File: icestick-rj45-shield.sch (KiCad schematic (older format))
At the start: 0 parts

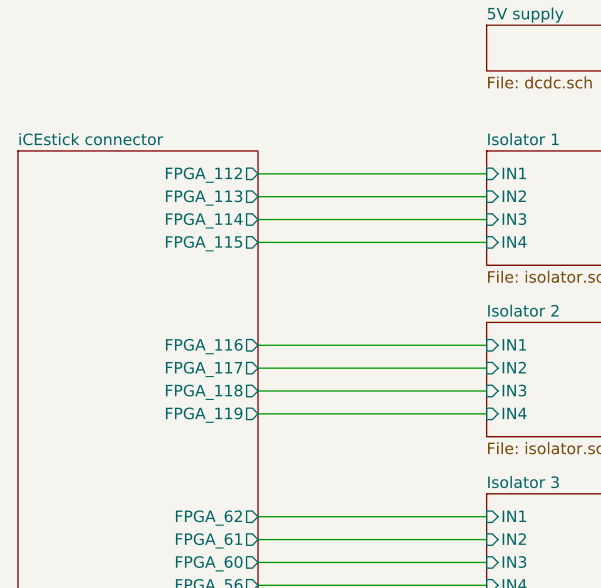
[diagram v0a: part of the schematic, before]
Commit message: Continued layouting
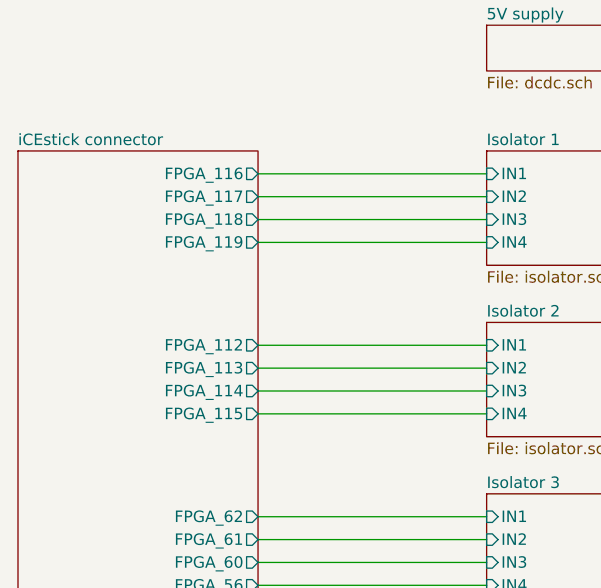
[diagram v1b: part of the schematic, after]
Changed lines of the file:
@@
 F0 "iCEstick connector" 50
 F1 "icestick.sch" 50
-F2 "FPGA_112" O R 4800 2500 50
-F3 "FPGA_113" O R 4800 2600 50
-F4 "FPGA_114" O R 4800 2700 50
-F5 "FPGA_115" O R 4800 2800 50
-F6 "FPGA_116" O R 4800 3250 50
-F7 "FPGA_117" O R 4800 3350 50
-F8 "FPGA_118" O R 4800 3450 50
-F9 "FPGA_119" O R 4800 3550 50
+F2 "FPGA_112" O R 4800 3250 50
+F3 "FPGA_113" O R 4800 3350 50
+F4 "FPGA_114" O R 4800 3450 50
+F5 "FPGA_115" O R 4800 3550 50
+F6 "FPGA_116" O R 4800 2500 50
+F7 "FPGA_117" O R 4800 2600 50
+F8 "FPGA_118" O R 4800 2700 50
+F9 "FPGA_119" O R 4800 2800 50
 F10 "FPGA_62" O R 4800 4000 50
 F11 "FPGA_61" O R 4800 4100 50

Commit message: Routed all the signals
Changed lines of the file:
@@
 F4 "FPGA_114" O R 4800 3450 50
 F5 "FPGA_115" O R 4800 3550 50
-F6 "FPGA_116" O R 4800 2500 50
-F7 "FPGA_117" O R 4800 2600 50
-F8 "FPGA_118" O R 4800 2700 50
-F9 "FPGA_119" O R 4800 2800 50
-F10 "FPGA_62" O R 4800 4000 50
-F11 "FPGA_61" O R 4800 4100 50
-F12 "FPGA_60" O R 4800 4200 50
-F13 "FPGA_56" O R 4800 4300 50
+F6 "FPGA_116" O R 4800 2800 50
+F7 "FPGA_117" O R 4800 2700 50
+F8 "FPGA_118" O R 4800 2600 50
+F9 "FPGA_119" O R 4800 2500 50
+F10 "FPGA_62" O R 4800 4300 50
+F11 "FPGA_61" O R 4800 4200 50
+F12 "FPGA_60" O R 4800 4100 50
+F13 "FPGA_56" O R 4800 4000 50
 F14 "FPGA_48" O R 4800 4750 50
 F15 "FPGA_47" O R 4800 4850 50

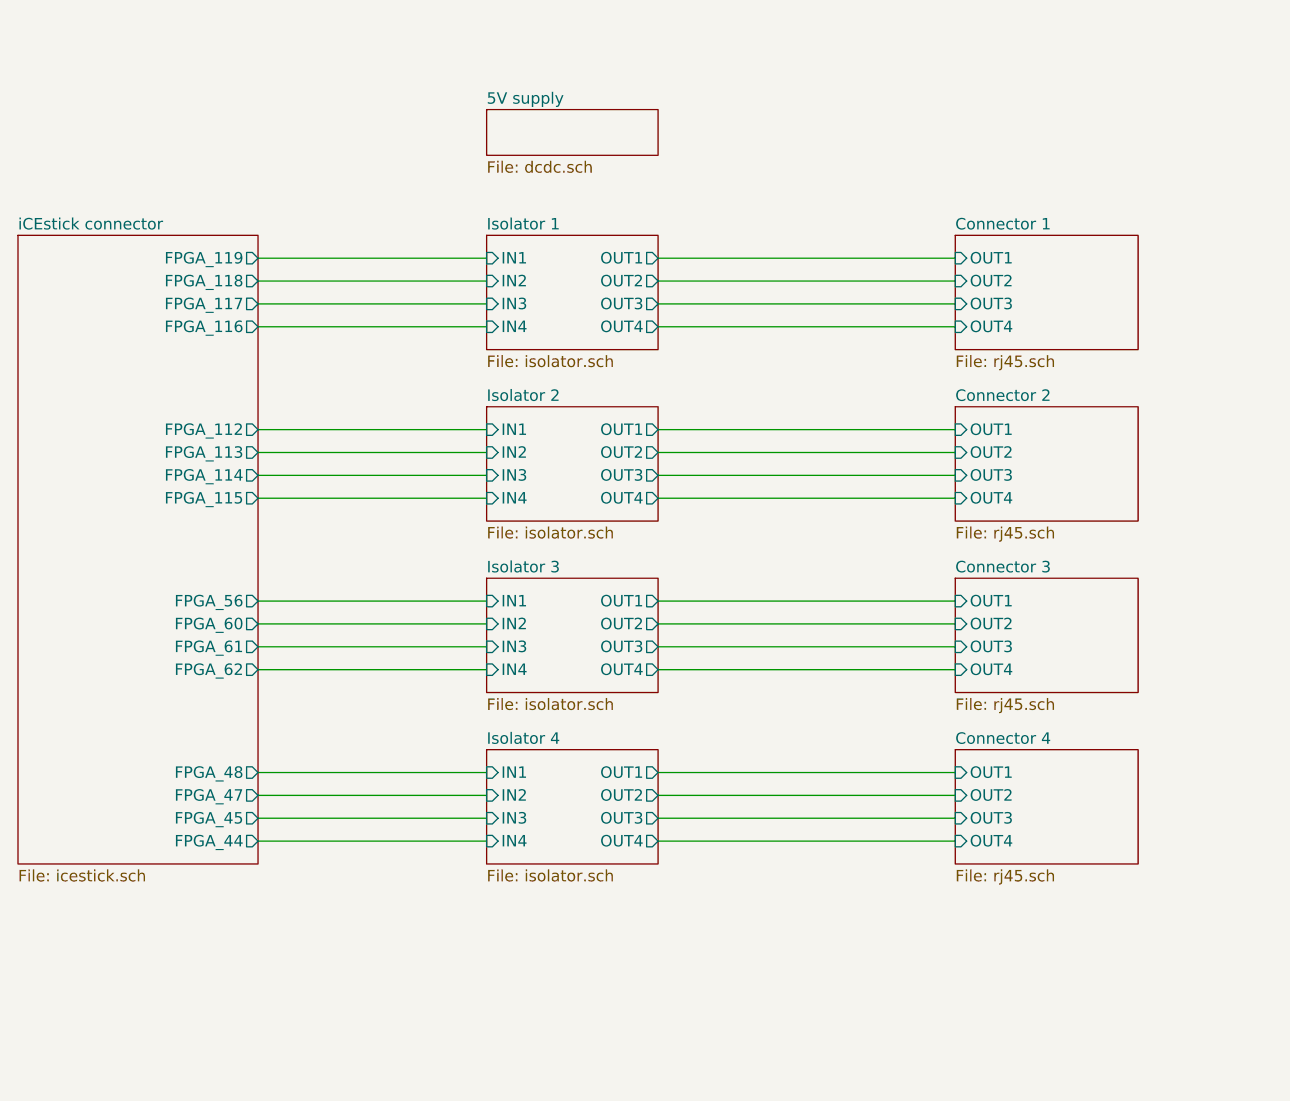
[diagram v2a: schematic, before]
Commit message: Updated RJ45 symbol and corresponding signal names
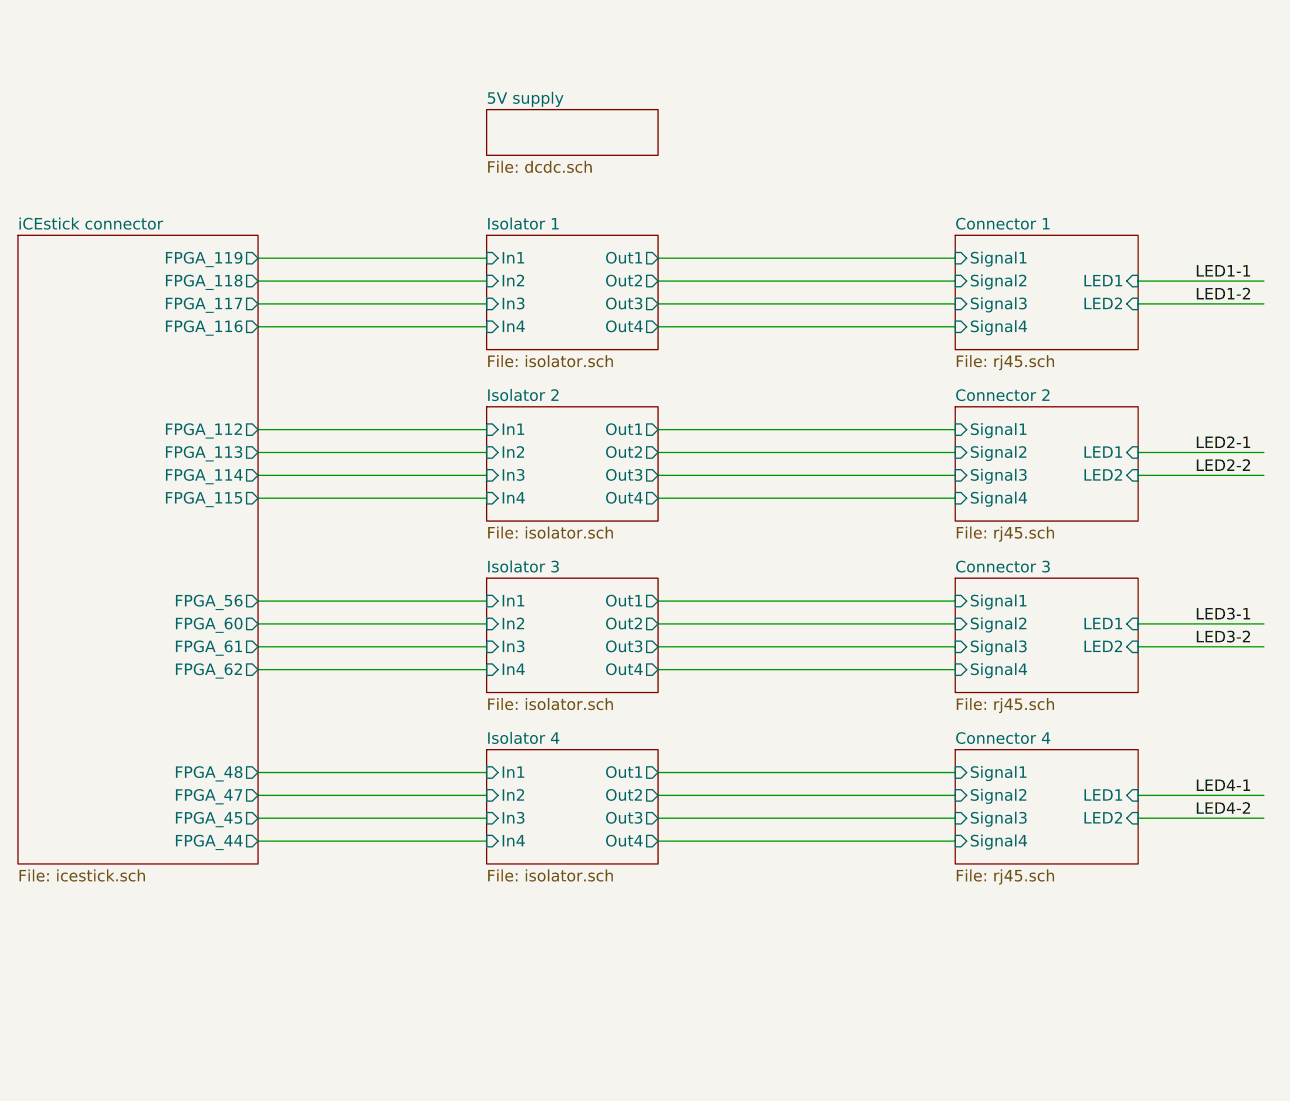
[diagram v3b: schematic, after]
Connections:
- net labels added: LED1-1, LED1-2, LED2-1, LED2-2, LED3-1, LED3-2, LED4-1, LED4-2
- wire segments 32 -> 40
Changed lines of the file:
@@
 F0 "Isolator 1" 50
 F1 "isolator.sch" 50
-F2 "IN1" I L 5800 2500 50
-F3 "IN2" I L 5800 2600 50
-F4 "OUT1" O R 6550 2500 50
-F5 "OUT2" O R 6550 2600 50
-F6 "OUT3" O R 6550 2700 50
-F7 "OUT4" O R 6550 2800 50
-F8 "IN3" I L 5800 2700 50
-F9 "IN4" I L 5800 2800 50
+F2 "In1" I L 5800 2500 50
+F3 "In2" I L 5800 2600 50
+F4 "Out1" O R 6550 2500 50
+F5 "Out2" O R 6550 2600 50
+F6 "Out3" O R 6550 2700 50
+F7 "Out4" O R 6550 2800 50
+F8 "In3" I L 5800 2700 50
+F9 "In4" I L 5800 2800 50
 $EndSheet
 $Sheet
@@
 F0 "Isolator 3" 50
 F1 "isolator.sch" 50
-F2 "IN1" I L 5800 4000 50
-F3 "IN2" I L 5800 4100 50
-F4 "OUT1" O R 6550 4000 50
-F5 "OUT2" O R 6550 4100 50
-F6 "OUT3" O R 6550 4200 50
-F7 "OUT4" O R 6550 4300 50
-F8 "IN3" I L 5800 4200 50
-F9 "IN4" I L 5800 4300 50
+F2 "In1" I L 5800 4000 50
+F3 "In2" I L 5800 4100 50
+F4 "Out1" O R 6550 4000 50
+F5 "Out2" O R 6550 4100 50
+F6 "Out3" O R 6550 4200 50
+F7 "Out4" O R 6550 4300 50
+F8 "In3" I L 5800 4200 50
+F9 "In4" I L 5800 4300 50
 $EndSheet
 $Sheet
@@
 F0 "Isolator 2" 50
 F1 "isolator.sch" 50
-F2 "IN1" I L 5800 3250 50
-F3 "IN2" I L 5800 3350 50
-F4 "OUT1" O R 6550 3250 50
-F5 "OUT2" O R 6550 3350 50
-F6 "OUT3" O R 6550 3450 50
-F7 "OUT4" O R 6550 3550 50
-F8 "IN3" I L 5800 3450 50
-F9 "IN4" I L 5800 3550 50
+F2 "In1" I L 5800 3250 50
+F3 "In2" I L 5800 3350 50
+F4 "Out1" O R 6550 3250 50
+F5 "Out2" O R 6550 3350 50
+F6 "Out3" O R 6550 3450 50
+F7 "Out4" O R 6550 3550 50
+F8 "In3" I L 5800 3450 50
+F9 "In4" I L 5800 3550 50
 $EndSheet
 $Sheet
@@
 F0 "Isolator 4" 50
 F1 "isolator.sch" 50
-F2 "IN1" I L 5800 4750 50
-F3 "IN2" I L 5800 4850 50
-F4 "OUT1" O R 6550 4750 50
-F5 "OUT2" O R 6550 4850 50
-F6 "OUT3" O R 6550 4950 50
-F7 "OUT4" O R 6550 5050 50
-F8 "IN3" I L 5800 4950 50
-F9 "IN4" I L 5800 5050 50
+F2 "In1" I L 5800 4750 50
+F3 "In2" I L 5800 4850 50
+F4 "Out1" O R 6550 4750 50
+F5 "Out2" O R 6550 4850 50
+F6 "Out3" O R 6550 4950 50
+F7 "Out4" O R 6550 5050 50
+F8 "In3" I L 5800 4950 50
+F9 "In4" I L 5800 5050 50
 $EndSheet
 Wire Wire Line
@@
 F0 "Connector 1" 50
 F1 "rj45.sch" 50
-F2 "OUT1" I L 7850 2500 50
-F3 "OUT2" I L 7850 2600 50
-F4 "OUT3" I L 7850 2700 50
-F5 "OUT4" I L 7850 2800 50
+F2 "Signal1" I L 7850 2500 50
+F3 "Signal2" I L 7850 2600 50
+F4 "Signal3" I L 7850 2700 50
+F5 "Signal4" I L 7850 2800 50
+F6 "LED1" I R 8650 2600 50
+F7 "LED2" I R 8650 2700 50
 $EndSheet
 Wire Wire Line
@@
 F0 "Connector 2" 50
 F1 "rj45.sch" 50
-F2 "OUT1" I L 7850 3250 50
-F3 "OUT2" I L 7850 3350 50
-F4 "OUT3" I L 7850 3450 50
-F5 "OUT4" I L 7850 3550 50
+F2 "Signal1" I L 7850 3250 50
+F3 "Signal2" I L 7850 3350 50
+F4 "Signal3" I L 7850 3450 50
+F5 "Signal4" I L 7850 3550 50
+F6 "LED1" I R 8650 3350 50
+F7 "LED2" I R 8650 3450 50
 $EndSheet
 Wire Wire Line
@@
 F0 "Connector 3" 50
 F1 "rj45.sch" 50
-F2 "OUT1" I L 7850 4000 50
-F3 "OUT2" I L 7850 4100 50
-F4 "OUT3" I L 7850 4200 50
-F5 "OUT4" I L 7850 4300 50
+F2 "Signal1" I L 7850 4000 50
+F3 "Signal2" I L 7850 4100 50
+F4 "Signal3" I L 7850 4200 50
+F5 "Signal4" I L 7850 4300 50
+F6 "LED1" I R 8650 4100 50
+F7 "LED2" I R 8650 4200 50
 $EndSheet
 Wire Wire Line
@@
 F0 "Connector 4" 50
 F1 "rj45.sch" 50
-F2 "OUT1" I L 7850 4750 50
-F3 "OUT2" I L 7850 4850 50
-F4 "OUT3" I L 7850 4950 50
-F5 "OUT4" I L 7850 5050 50
+F2 "Signal1" I L 7850 4750 50
+F3 "Signal2" I L 7850 4850 50
+F4 "Signal3" I L 7850 4950 50
+F5 "Signal4" I L 7850 5050 50
+F6 "LED1" I R 8650 4850 50
+F7 "LED2" I R 8650 4950 50
 $EndSheet
 Wire Wire Line
@@
 Wire Wire Line
 	6550 4750 7850 4750
+Wire Wire Line
+	8650 2600 9200 2600
+Wire Wire Line
+	8650 2700 9200 2700
+Wire Wire Line
+	8650 3350 9200 3350
+Wire Wire Line
+	8650 3450 9200 3450
+Wire Wire Line
+	8650 4100 9200 4100
+Wire Wire Line
+	8650 4200 9200 4200
+Wire Wire Line
+	8650 4850 9200 4850
+Wire Wire Line
+	8650 4950 9200 4950
+Text Label 8900 2600 0    50   ~ 0
+LED1-1
+Text Label 8900 2700 0    50   ~ 0
+LED1-2
+Text Label 8900 3350 0    50   ~ 0
+LED2-1
+Text Label 8900 3450 0    50   ~ 0
+LED2-2
+Text Label 8900 4100 0    50   ~ 0
+LED3-1
+Text Label 8900 4200 0    50   ~ 0
+LED3-2
+Text Label 8900 4850 0    50   ~ 0
+LED4-1
+Text Label 8900 4950 0    50   ~ 0
+LED4-2
 $EndSCHEMATC

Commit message: Began redesigning with Si8660
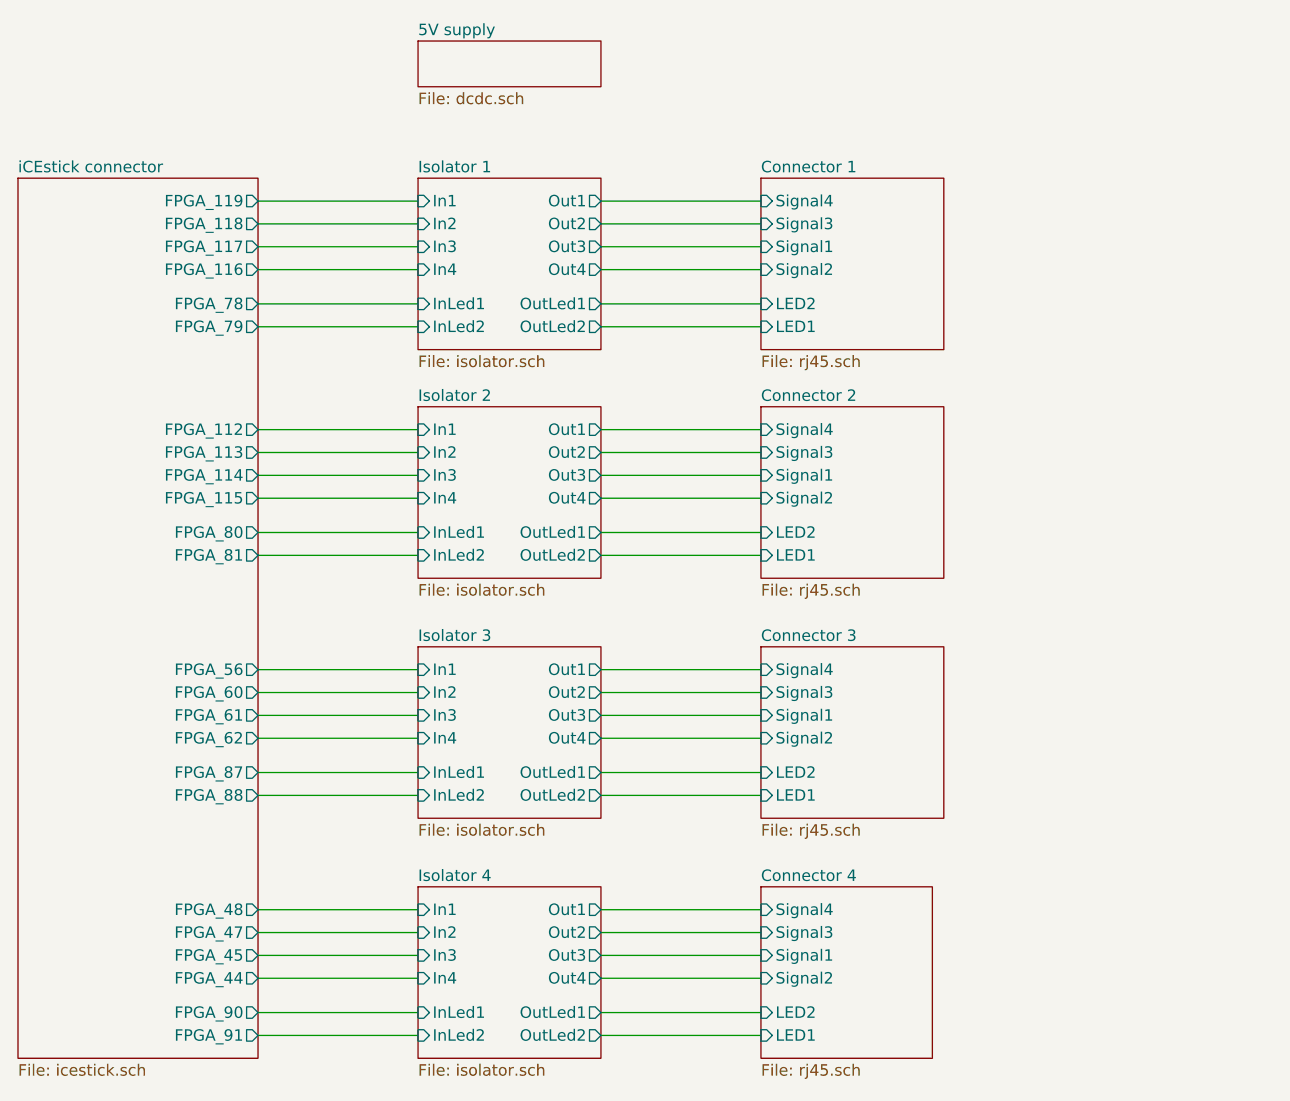
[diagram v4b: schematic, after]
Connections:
- net labels removed: LED1-1, LED1-2, LED2-1, LED2-2, LED3-1, LED3-2, LED4-1, LED4-2
- wire segments 40 -> 48

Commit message: Finished layout with 4x Si8660
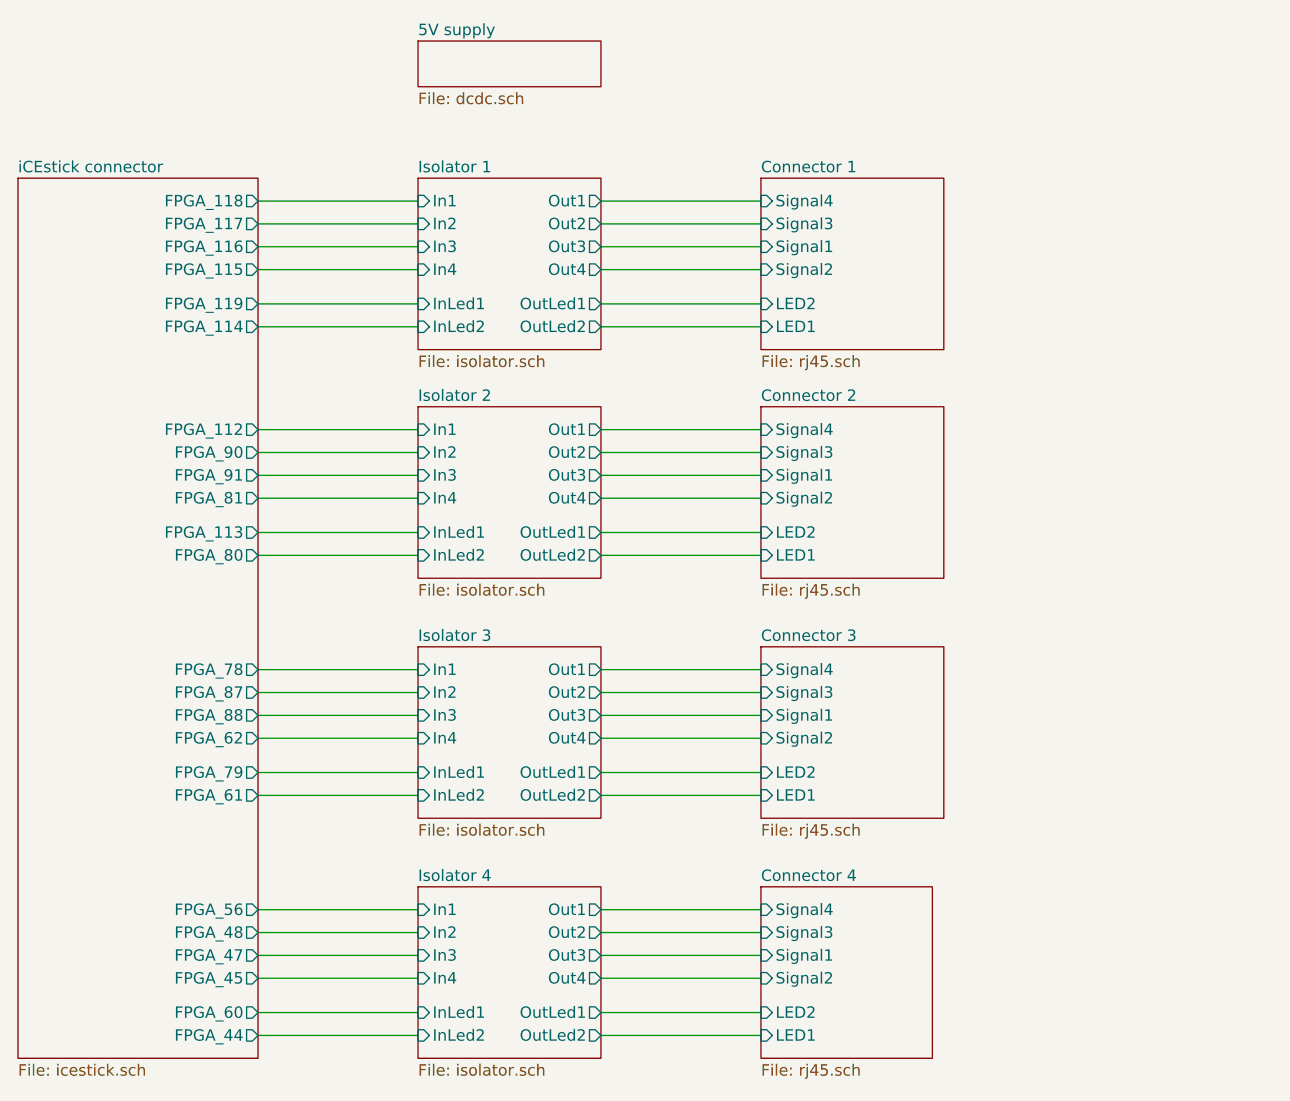
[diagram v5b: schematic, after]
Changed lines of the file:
@@
 F1 "icestick.sch" 50
 F2 "FPGA_112" O R 4800 3250 50
-F3 "FPGA_113" O R 4800 3350 50
-F4 "FPGA_114" O R 4800 3450 50
-F5 "FPGA_115" O R 4800 3550 50
-F6 "FPGA_116" O R 4800 2550 50
-F7 "FPGA_117" O R 4800 2450 50
-F8 "FPGA_118" O R 4800 2350 50
-F9 "FPGA_119" O R 4800 2250 50
+F3 "FPGA_113" O R 4800 3700 50
+F4 "FPGA_114" O R 4800 2800 50
+F5 "FPGA_115" O R 4800 2550 50
+F6 "FPGA_116" O R 4800 2450 50
+F7 "FPGA_117" O R 4800 2350 50
+F8 "FPGA_118" O R 4800 2250 50
+F9 "FPGA_119" O R 4800 2700 50
 F10 "FPGA_62" O R 4800 4600 50
-F11 "FPGA_61" O R 4800 4500 50
-F12 "FPGA_60" O R 4800 4400 50
-F13 "FPGA_56" O R 4800 4300 50
-F14 "FPGA_48" O R 4800 5350 50
-F15 "FPGA_47" O R 4800 5450 50
-F16 "FPGA_45" O R 4800 5550 50
-F17 "FPGA_44" O R 4800 5650 50
-F18 "FPGA_78" O R 4800 2700 50
-F19 "FPGA_79" O R 4800 2800 50
-F20 "FPGA_80" O R 4800 3700 50
-F21 "FPGA_81" O R 4800 3800 50
-F22 "FPGA_87" O R 4800 4750 50
-F23 "FPGA_88" O R 4800 4850 50
-F24 "FPGA_90" O R 4800 5800 50
-F25 "FPGA_91" O R 4800 5900 50
+F11 "FPGA_61" O R 4800 4850 50
+F12 "FPGA_60" O R 4800 5800 50
+F13 "FPGA_56" O R 4800 5350 50
+F14 "FPGA_48" O R 4800 5450 50
+F15 "FPGA_47" O R 4800 5550 50
+F16 "FPGA_45" O R 4800 5650 50
+F17 "FPGA_44" O R 4800 5900 50
+F18 "FPGA_78" O R 4800 4300 50
+F19 "FPGA_79" O R 4800 4750 50
+F20 "FPGA_80" O R 4800 3800 50
+F21 "FPGA_81" O R 4800 3550 50
+F22 "FPGA_87" O R 4800 4400 50
+F23 "FPGA_88" O R 4800 4500 50
+F24 "FPGA_90" O R 4800 3350 50
+F25 "FPGA_91" O R 4800 3450 50
 $EndSheet
 Wire Wire Line
